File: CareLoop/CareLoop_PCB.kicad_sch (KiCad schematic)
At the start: 0 parts

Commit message: updated version
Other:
- added sheet Antenna (antenna.kicad_sch)
- sheet Battery ports: added Dminus, Dplus; removed none
- sheet MAX30102 ports: added MAX_INT; removed none
- sheet MCU ports: added ANT, Dminus, Dplus, INT_MAX; removed none
- sheet MPU6050 ports: added INT_MPU; removed INT

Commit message: WP: update Schematics
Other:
- sheet Battery ports: added VBUS, VCC; removed Vout
- sheet MCU ports: added VBUS; removed none
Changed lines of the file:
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@@
+	(wire
+		(pts
+			(xy 71.12 60.96) (xy 71.12 107.95)
+		)
+		(stroke
+			(width 0)
+			(type default)
+		)
+	)
 	(wire
 		(pts
@@
 	(wire
 		(pts
+			(xy 190.5 88.9) (xy 199.39 88.9)
+		)
+		(stroke
+			(width 0)
+			(type default)
+		)
+	)
+	(wire
+		(pts
 			(xy 173.99 92.71) (xy 129.54 92.71)
 		)
@@
 	(wire
 		(pts
+			(xy 199.39 60.96) (xy 71.12 60.96)
+		)
+		(stroke
+			(width 0)
+			(type default)
+		)
+	)
+	(wire
+		(pts
 			(xy 173.99 109.22) (xy 142.24 109.22)
 		)
@@
 		(pts
 			(xy 189.23 109.22) (xy 190.5 109.22)
+		)
+		(stroke
+			(width 0)
+			(type default)
+		)
+	)
+	(wire
+		(pts
+			(xy 199.39 88.9) (xy 199.39 60.96)
+		)
+		(stroke
+			(width 0)
+			(type default)
+		)
+	)
+	(wire
+		(pts
+			(xy 71.12 107.95) (xy 96.52 107.95)
 		)
 		(stroke
@@
 			)
 		)
-		(pin "Vout" output
-			(at 190.5 91.44 0)
-			(effects
-				(font
-					(size 1.27 1.27)
-				)
-				(justify right)
-			)
-		)
 		(pin "Dminus" bidirectional
 			(at 173.99 90.17 180)
@@
 				)
 				(justify left)
+			)
+		)
+		(pin "VCC" output
+			(at 190.5 91.44 0)
+			(effects
+				(font
+					(size 1.27 1.27)
+				)
+				(justify right)
+			)
+		)
+		(pin "VBUS" output
+			(at 190.5 88.9 0)
+			(effects
+				(font
+					(size 1.27 1.27)
+				)
+				(justify right)
 			)
 		)
@@
 			)
 		)
+		(pin "VBUS" input
+			(at 96.52 107.95 180)
+			(effects
+				(font
+					(size 1.27 1.27)
+				)
+				(justify left)
+			)
+		)

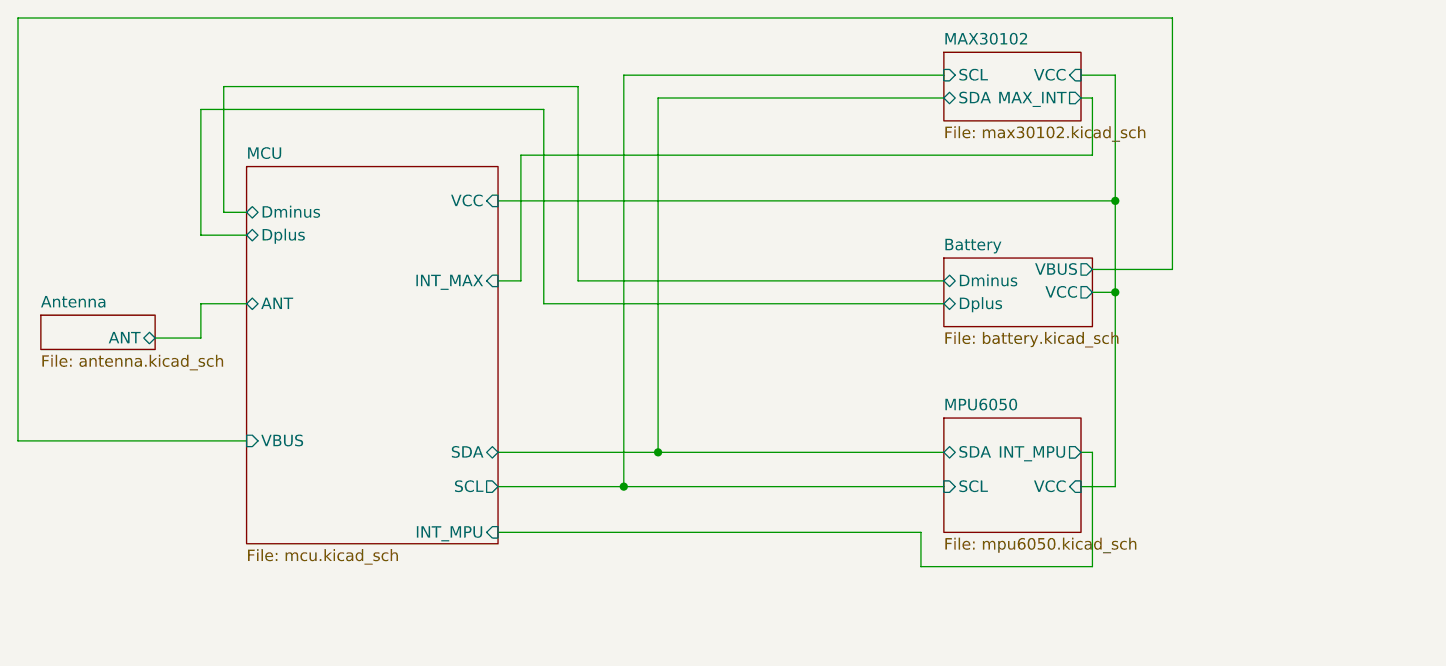
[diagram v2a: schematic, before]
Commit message: WP: Placement PCB Parts done
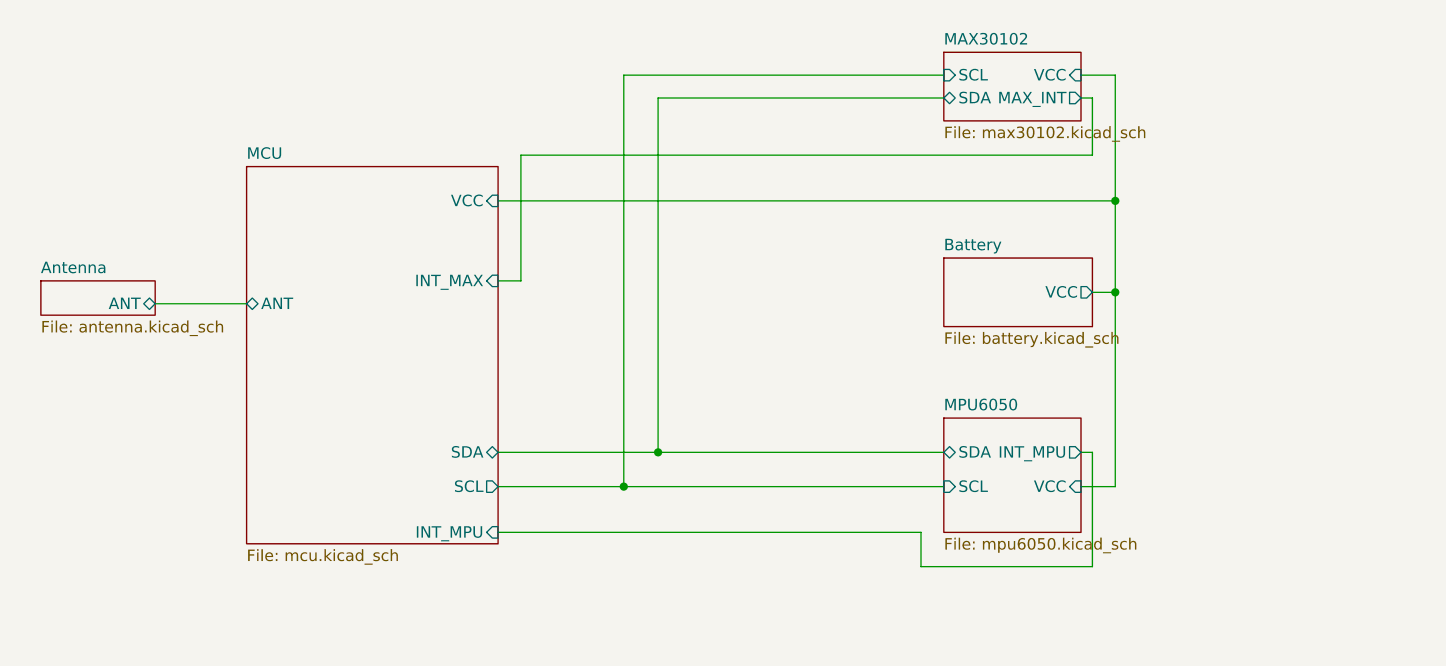
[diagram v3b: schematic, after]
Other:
- sheet Battery ports: added none; removed Dminus, Dplus, VBUS
- sheet MCU ports: added none; removed Dminus, Dplus, VBUS
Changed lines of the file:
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@@
-	(wire
-		(pts
-			(xy 91.44 96.52) (xy 91.44 92.71)
-		)
-		(stroke
-			(width 0)
-			(type default)
-		)
-	)
-	(wire
-		(pts
-			(xy 129.54 92.71) (xy 129.54 71.12)
-		)
-		(stroke
-			(width 0)
-			(type default)
-		)
-	)
-	(wire
-		(pts
-			(xy 93.98 82.55) (xy 96.52 82.55)
-		)
-		(stroke
-			(width 0)
-			(type default)
-		)
-	)
 	(wire
 		(pts
@@
 	(wire
 		(pts
-			(xy 129.54 71.12) (xy 91.44 71.12)
-		)
-		(stroke
-			(width 0)
-			(type default)
-		)
-	)
-	(wire
-		(pts
-			(xy 93.98 68.58) (xy 93.98 82.55)
-		)
-		(stroke
-			(width 0)
-			(type default)
-		)
-	)
-	(wire
-		(pts
 			(xy 124.46 118.11) (xy 171.45 118.11)
 		)
@@
 	(wire
 		(pts
-			(xy 71.12 60.96) (xy 71.12 107.95)
-		)
-		(stroke
-			(width 0)
-			(type default)
-		)
-	)
-	(wire
-		(pts
 			(xy 124.46 113.03) (xy 138.43 113.03)
 		)
@@
 	(wire
 		(pts
-			(xy 86.36 96.52) (xy 91.44 96.52)
+			(xy 86.36 92.71) (xy 96.52 92.71)
 		)
 		(stroke
@@
 	(wire
 		(pts
-			(xy 133.35 68.58) (xy 93.98 68.58)
-		)
-		(stroke
-			(width 0)
-			(type default)
-		)
-	)
-	(wire
-		(pts
 			(xy 189.23 69.85) (xy 190.5 69.85)
 		)
@@
 	(wire
 		(pts
-			(xy 133.35 68.58) (xy 133.35 90.17)
-		)
-		(stroke
-			(width 0)
-			(type default)
-		)
-	)
-	(wire
-		(pts
 			(xy 124.46 109.22) (xy 142.24 109.22)
 		)
@@
 	(wire
 		(pts
-			(xy 91.44 92.71) (xy 96.52 92.71)
-		)
-		(stroke
-			(width 0)
-			(type default)
-		)
-	)
-	(wire
-		(pts
 			(xy 124.46 81.28) (xy 193.04 81.28)
 		)
@@
 	(wire
 		(pts
-			(xy 91.44 85.09) (xy 96.52 85.09)
-		)
-		(stroke
-			(width 0)
-			(type default)
-		)
-	)
-	(wire
-		(pts
-			(xy 133.35 90.17) (xy 173.99 90.17)
-		)
-		(stroke
-			(width 0)
-			(type default)
-		)
-	)
-	(wire
-		(pts
-			(xy 190.5 88.9) (xy 199.39 88.9)
-		)
-		(stroke
-			(width 0)
-			(type default)
-		)
-	)
-	(wire
-		(pts
-			(xy 173.99 92.71) (xy 129.54 92.71)
-		)
-		(stroke
-			(width 0)
-			(type default)
-		)
-	)
-	(wire
-		(pts
-			(xy 199.39 60.96) (xy 71.12 60.96)
-		)
-		(stroke
-			(width 0)
-			(type default)
-		)
-	)
-	(wire
-		(pts
 			(xy 173.99 109.22) (xy 142.24 109.22)
 		)
@@
 		(pts
 			(xy 189.23 109.22) (xy 190.5 109.22)
-		)
-		(stroke
-			(width 0)
-			(type default)
-		)
-	)
-	(wire
-		(pts
-			(xy 199.39 88.9) (xy 199.39 60.96)
-		)
-		(stroke
-			(width 0)
-			(type default)
-		)
-	)
-	(wire
-		(pts
-			(xy 71.12 107.95) (xy 96.52 107.95)
-		)
-		(stroke
-			(width 0)
-			(type default)
-		)
-	)
-	(wire
-		(pts
-			(xy 91.44 71.12) (xy 91.44 85.09)
 		)
 		(stroke
@@
 			)
 		)
-		(pin "Dminus" bidirectional
-			(at 173.99 90.17 180)
-			(effects
-				(font
-					(size 1.27 1.27)
-				)
-				(justify left)
-			)
-		)
-		(pin "Dplus" bidirectional
-			(at 173.99 92.71 180)
-			(effects
-				(font
-					(size 1.27 1.27)
-				)
-				(justify left)
-			)
-		)
 		(pin "VCC" output
 			(at 190.5 91.44 0)
-			(effects
-				(font
-					(size 1.27 1.27)
-				)
-				(justify right)
-			)
-		)
-		(pin "VBUS" output
-			(at 190.5 88.9 0)
 			(effects
 				(font
@@
 	)
 	(sheet
-		(at 73.66 93.98)
+		(at 73.66 90.17)
 		(size 12.7 3.81)
 		(exclude_from_sim no)
@@
 		)
 		(property "Sheetname" "Antenna"
-			(at 73.66 93.2684 0)
+			(at 73.66 89.4584 0)
 			(effects
 				(font
@@
 		)
 		(property "Sheetfile" "antenna.kicad_sch"
-			(at 73.66 98.3746 0)
+			(at 73.66 94.5646 0)
 			(effects
 				(font
@@
 		)
 		(property "Field2" ""
-			(at 73.66 93.98 0)
+			(at 73.66 90.17 0)
 			(effects
 				(font
@@
 		)
 		(pin "ANT" bidirectional
-			(at 86.36 96.52 0)
+			(at 86.36 92.71 0)
 			(effects
 				(font
@@
 			)
 		)
-		(pin "Dminus" bidirectional
-			(at 96.52 82.55 180)
-			(effects
-				(font
-					(size 1.27 1.27)
-				)
-				(justify left)
-			)
-		)
-		(pin "Dplus" bidirectional
-			(at 96.52 85.09 180)
-			(effects
-				(font
-					(size 1.27 1.27)
-				)
-				(justify left)
-			)
-		)
 		(pin "INT_MAX" input
 			(at 124.46 90.17 0)
@@
 			)
 		)
-		(pin "VBUS" input
-			(at 96.52 107.95 180)
-			(effects
-				(font
-					(size 1.27 1.27)
-				)
-				(justify left)
-			)
-		)

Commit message: update Voltagedevider
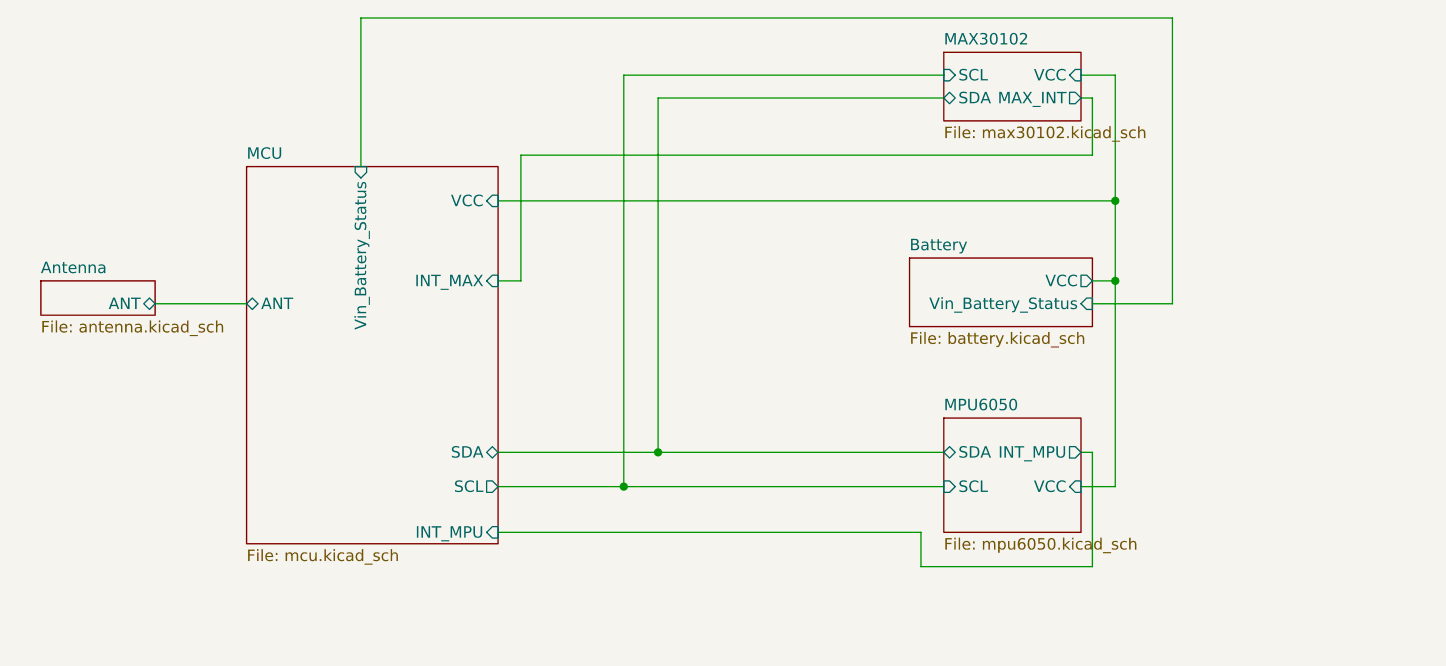
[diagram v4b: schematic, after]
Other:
- sheet Battery ports: added Vin_Battery_Status; removed none
- sheet MCU ports: added Vin_Battery_Status; removed none
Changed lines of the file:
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@@
 	(paper "A4")
+	(junction
+		(at 193.04 90.17)
+		(diameter 0)
+		(color 0 0 0 0)
+	)
 	(junction
 		(at 142.24 109.22)
@@
 	)
 	(junction
-		(at 193.04 91.44)
-		(diameter 0)
-		(color 0 0 0 0)
-	)
-	(junction
 		(at 138.43 113.03)
 		(diameter 0)
@@
 	(wire
 		(pts
-			(xy 190.5 91.44) (xy 193.04 91.44)
+			(xy 190.5 90.17) (xy 193.04 90.17)
+		)
+		(stroke
+			(width 0)
+			(type default)
+		)
+	)
+	(wire
+		(pts
+			(xy 109.22 60.96) (xy 109.22 77.47)
 		)
 		(stroke
@@
 	(wire
 		(pts
+			(xy 190.5 92.71) (xy 199.39 92.71)
+		)
+		(stroke
+			(width 0)
+			(type default)
+		)
+	)
+	(wire
+		(pts
+			(xy 199.39 60.96) (xy 109.22 60.96)
+		)
+		(stroke
+			(width 0)
+			(type default)
+		)
+	)
+	(wire
+		(pts
 			(xy 124.46 118.11) (xy 171.45 118.11)
 		)
@@
 	(wire
 		(pts
+			(xy 199.39 92.71) (xy 199.39 60.96)
+		)
+		(stroke
+			(width 0)
+			(type default)
+		)
+	)
+	(wire
+		(pts
 			(xy 189.23 67.31) (xy 193.04 67.31)
 		)
@@
 	(wire
 		(pts
+			(xy 193.04 90.17) (xy 193.04 113.03)
+		)
+		(stroke
+			(width 0)
+			(type default)
+		)
+	)
+	(wire
+		(pts
 			(xy 193.04 113.03) (xy 189.23 113.03)
 		)
@@
 	(wire
 		(pts
-			(xy 193.04 81.28) (xy 193.04 91.44)
+			(xy 193.04 81.28) (xy 193.04 90.17)
 		)
 		(stroke
@@
 	(wire
 		(pts
-			(xy 193.04 91.44) (xy 193.04 113.03)
-		)
-		(stroke
-			(width 0)
-			(type default)
-		)
-	)
-	(wire
-		(pts
 			(xy 171.45 121.92) (xy 190.5 121.92)
 		)
@@
 	)
 	(sheet
-		(at 173.99 87.63)
-		(size 16.51 7.62)
+		(at 170.18 87.63)
+		(size 20.32 7.62)
 		(exclude_from_sim no)
 		(in_bom yes)
@@
 		)
 		(property "Sheetname" "Battery"
-			(at 173.99 86.9184 0)
+			(at 170.18 86.9184 0)
 			(effects
 				(font
@@
 		)
 		(property "Sheetfile" "battery.kicad_sch"
-			(at 173.99 95.8346 0)
+			(at 170.18 95.8346 0)
 			(effects
 				(font
@@
 		)
 		(pin "VCC" output
-			(at 190.5 91.44 0)
+			(at 190.5 90.17 0)
+			(effects
+				(font
+					(size 1.27 1.27)
+				)
+				(justify right)
+			)
+		)
+		(pin "Vin_Battery_Status" input
+			(at 190.5 92.71 0)
 			(effects
 				(font
@@
 			(effects
 				(font
+					(size 1.27 1.27)
+				)
+				(justify right)
+			)
+		)
+		(pin "Vin_Battery_Status" input
+			(at 109.22 77.47 90)
+			(effects
+				(font
